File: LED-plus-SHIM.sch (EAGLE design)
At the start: 304 parts, among them IC1 TXB0101DCKR

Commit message: Fixed some texts
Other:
- note added: "PI-LEDPS-0010"
- note added: "Pi Plus sized LED-SHIM for Pi's 40-pin extension slot (c) Andriy Golovnya"
- note removed: "PI-LEDZS-0010"
- note removed: "Pi Zero sized LED-SHIM for Pi's 40-pin extension slot (c) Andriy Golovnya"
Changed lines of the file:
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@@
 <plain>
 <text x="256.54" y="7.62" size="2.54" layer="94">1.0</text>
-<text x="198.12" y="7.62" size="2.54" layer="94">PI-LEDZS-0010</text>
-<text x="165.1" y="25.4" size="2.54" layer="94">Pi Zero sized LED-SHIM for Pi's 40-pin extension slot
+<text x="198.12" y="7.62" size="2.54" layer="94">PI-LEDPS-0010</text>
+<text x="165.1" y="25.4" size="2.54" layer="94">Pi Plus sized LED-SHIM for Pi's 40-pin extension slot
 (c) Andriy Golovnya</text>
 <text x="25.4" y="121.92" size="2.54" layer="94">Right connector
@@
 <plain>
 <text x="256.54" y="7.62" size="2.54" layer="94">1.0</text>
-<text x="198.12" y="7.62" size="2.54" layer="94">PI-LEDZS-0010</text>
-<text x="165.1" y="25.4" size="2.54" layer="94">Pi Zero sized LED-SHIM for Pi's 40-pin extension slot
+<text x="198.12" y="7.62" size="2.54" layer="94">PI-LEDPS-0010</text>
+<text x="165.1" y="25.4" size="2.54" layer="94">Pi Plus sized LED-SHIM for Pi's 40-pin extension slot
 (c) Andriy Golovnya</text>
 <text x="10.16" y="86.36" size="1.778" layer="97">Following configurations are supported:
@@
 <plain>
 <text x="256.54" y="7.62" size="2.54" layer="94">1.0</text>
-<text x="198.12" y="7.62" size="2.54" layer="94">PI-LEDZS-0010</text>
-<text x="165.1" y="25.4" size="2.54" layer="94">Pi Zero sized LED-SHIM for Pi's 40-pin extension slot
+<text x="198.12" y="7.62" size="2.54" layer="94">PI-LEDPS-0010</text>
+<text x="165.1" y="25.4" size="2.54" layer="94">Pi Plus sized LED-SHIM for Pi's 40-pin extension slot
 (c) Andriy Golovnya</text>
 </plain>
@@
 <plain>
 <text x="256.54" y="7.62" size="2.54" layer="94">1.0</text>
-<text x="198.12" y="7.62" size="2.54" layer="94">PI-LEDZS-0010</text>
-<text x="165.1" y="25.4" size="2.54" layer="94">Pi Zero sized LED-SHIM for Pi's 40-pin extension slot
+<text x="198.12" y="7.62" size="2.54" layer="94">PI-LEDPS-0010</text>
+<text x="165.1" y="25.4" size="2.54" layer="94">Pi Plus sized LED-SHIM for Pi's 40-pin extension slot
 (c) Andriy Golovnya</text>
 </plain>

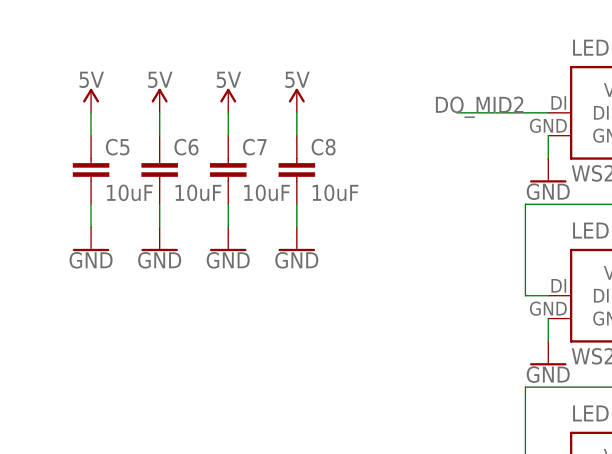
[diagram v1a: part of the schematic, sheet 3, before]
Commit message: Finished tracing plus SHIM board.
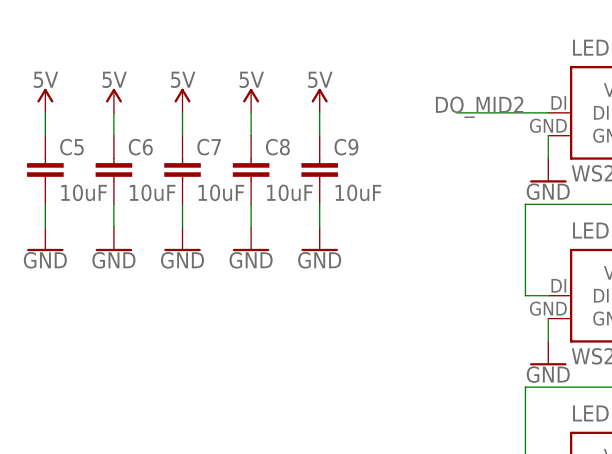
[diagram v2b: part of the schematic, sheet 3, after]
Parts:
- added C9: 10uF, rcl:C-EUC0805
- LOGO1: value MFDECLOGO_L_30MM -> MFDECLOGO_L_40MM; device _my_logos:MFDECLOGO_L_30MM -> _my_logos:MFDECLOGO_L_40MM
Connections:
- net 5V: now also C9.1
- net GND: now also C9.2
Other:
- moved on the sheet: C5, C6, C7, C8
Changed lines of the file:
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@@
 <parts>
 <part name="FRAME1" library="frames" library_urn="urn:adsk.eagle:library:229" deviceset="DINA4_L" device=""/>
-<part name="LOGO1" library="_my_logos" deviceset="MFDECLOGO" device="_L_30MM"/>
+<part name="LOGO1" library="_my_logos" deviceset="MFDECLOGO" device="_L_40MM" value="MFDECLOGO_L_40MM"/>
 <part name="SUPPLY1" library="SparkFun-PowerSymbols" library_urn="urn:adsk.eagle:library:530" deviceset="5V" device=""/>
 <part name="GND1" library="SparkFun-PowerSymbols" library_urn="urn:adsk.eagle:library:530" deviceset="GND" device=""/>
@@
 <part name="SUPPLY304" library="SparkFun-PowerSymbols" library_urn="urn:adsk.eagle:library:530" deviceset="5V" device=""/>
 <part name="GND301" library="SparkFun-PowerSymbols" library_urn="urn:adsk.eagle:library:530" deviceset="GND" device=""/>
+<part name="C9" library="rcl" library_urn="urn:adsk.eagle:library:334" deviceset="C-EU" device="C0805" package3d_urn="urn:adsk.eagle:package:23617/2" value="10uF"/>
+<part name="SUPPLY305" library="SparkFun-PowerSymbols" library_urn="urn:adsk.eagle:library:530" deviceset="5V" device=""/>
+<part name="GND302" library="SparkFun-PowerSymbols" library_urn="urn:adsk.eagle:library:530" deviceset="GND" device=""/>
 </parts>
 <sheets>
@@
 <attribute name="VALUE" x="124.46" y="9.906" size="1.778" layer="96" align="top-center"/>
 </instance>
-<instance part="C5" gate="G$1" x="20.32" y="154.94" smashed="yes">
-<attribute name="NAME" x="21.844" y="155.321" size="1.778" layer="95"/>
-<attribute name="VALUE" x="21.844" y="150.241" size="1.778" layer="96"/>
+<instance part="C5" gate="G$1" x="15.24" y="154.94" smashed="yes">
+<attribute name="NAME" x="16.764" y="155.321" size="1.778" layer="95"/>
+<attribute name="VALUE" x="16.764" y="150.241" size="1.778" layer="96"/>
 </instance>
-<instance part="SUPPLY301" gate="G$1" x="20.32" y="160.02" smashed="yes">
-<attribute name="VALUE" x="20.32" y="162.814" size="1.778" layer="96" align="bottom-center"/>
+<instance part="SUPPLY301" gate="G$1" x="15.24" y="160.02" smashed="yes">
+<attribute name="VALUE" x="15.24" y="162.814" size="1.778" layer="96" align="bottom-center"/>
 </instance>
-<instance part="GND298" gate="1" x="20.32" y="144.78" smashed="yes">
-<attribute name="VALUE" x="20.32" y="144.526" size="1.778" layer="96" align="top-center"/>
+<instance part="GND298" gate="1" x="15.24" y="144.78" smashed="yes">
+<attribute name="VALUE" x="15.24" y="144.526" size="1.778" layer="96" align="top-center"/>
 </instance>
-<instance part="C6" gate="G$1" x="27.94" y="154.94" smashed="yes">
-<attribute name="NAME" x="29.464" y="155.321" size="1.778" layer="95"/>
-<attribute name="VALUE" x="29.464" y="150.241" size="1.778" layer="96"/>
+<instance part="C6" gate="G$1" x="22.86" y="154.94" smashed="yes">
+<attribute name="NAME" x="24.384" y="155.321" size="1.778" layer="95"/>
+<attribute name="VALUE" x="24.384" y="150.241" size="1.778" layer="96"/>
 </instance>
-<instance part="SUPPLY302" gate="G$1" x="27.94" y="160.02" smashed="yes">
-<attribute name="VALUE" x="27.94" y="162.814" size="1.778" layer="96" align="bottom-center"/>
+<instance part="SUPPLY302" gate="G$1" x="22.86" y="160.02" smashed="yes">
+<attribute name="VALUE" x="22.86" y="162.814" size="1.778" layer="96" align="bottom-center"/>
 </instance>
-<instance part="GND299" gate="1" x="27.94" y="144.78" smashed="yes">
-<attribute name="VALUE" x="27.94" y="144.526" size="1.778" layer="96" align="top-center"/>
+<instance part="GND299" gate="1" x="22.86" y="144.78" smashed="yes">
+<attribute name="VALUE" x="22.86" y="144.526" size="1.778" layer="96" align="top-center"/>
 </instance>
-<instance part="C7" gate="G$1" x="35.56" y="154.94" smashed="yes">
-<attribute name="NAME" x="37.084" y="155.321" size="1.778" layer="95"/>
-<attribute name="VALUE" x="37.084" y="150.241" size="1.778" layer="96"/>
+<instance part="C7" gate="G$1" x="30.48" y="154.94" smashed="yes">
+<attribute name="NAME" x="32.004" y="155.321" size="1.778" layer="95"/>
+<attribute name="VALUE" x="32.004" y="150.241" size="1.778" layer="96"/>
 </instance>
-<instance part="SUPPLY303" gate="G$1" x="35.56" y="160.02" smashed="yes">
-<attribute name="VALUE" x="35.56" y="162.814" size="1.778" layer="96" align="bottom-center"/>
+<instance part="SUPPLY303" gate="G$1" x="30.48" y="160.02" smashed="yes">
+<attribute name="VALUE" x="30.48" y="162.814" size="1.778" layer="96" align="bottom-center"/>
 </instance>
-<instance part="GND300" gate="1" x="35.56" y="144.78" smashed="yes">
-<attribute name="VALUE" x="35.56" y="144.526" size="1.778" layer="96" align="top-center"/>
+<instance part="GND300" gate="1" x="30.48" y="144.78" smashed="yes">
+<attribute name="VALUE" x="30.48" y="144.526" size="1.778" layer="96" align="top-center"/>
 </instance>
-<instance part="C8" gate="G$1" x="43.18" y="154.94" smashed="yes">
-<attribute name="NAME" x="44.704" y="155.321" size="1.778" layer="95"/>
-<attribute name="VALUE" x="44.704" y="150.241" size="1.778" layer="96"/>
+<instance part="C8" gate="G$1" x="38.1" y="154.94" smashed="yes">
+<attribute name="NAME" x="39.624" y="155.321" size="1.778" layer="95"/>
+<attribute name="VALUE" x="39.624" y="150.241" size="1.778" layer="96"/>
 </instance>
-<instance part="SUPPLY304" gate="G$1" x="43.18" y="160.02" smashed="yes">
-<attribute name="VALUE" x="43.18" y="162.814" size="1.778" layer="96" align="bottom-center"/>
+<instance part="SUPPLY304" gate="G$1" x="38.1" y="160.02" smashed="yes">
+<attribute name="VALUE" x="38.1" y="162.814" size="1.778" layer="96" align="bottom-center"/>
 </instance>
-<instance part="GND301" gate="1" x="43.18" y="144.78" smashed="yes">
-<attribute name="VALUE" x="43.18" y="144.526" size="1.778" layer="96" align="top-center"/>
+<instance part="GND301" gate="1" x="38.1" y="144.78" smashed="yes">
+<attribute name="VALUE" x="38.1" y="144.526" size="1.778" layer="96" align="top-center"/>
+</instance>
+<instance part="C9" gate="G$1" x="45.72" y="154.94" smashed="yes">
+<attribute name="NAME" x="47.244" y="155.321" size="1.778" layer="95"/>
+<attribute name="VALUE" x="47.244" y="150.241" size="1.778" layer="96"/>
+</instance>
+<instance part="SUPPLY305" gate="G$1" x="45.72" y="160.02" smashed="yes">
+<attribute name="VALUE" x="45.72" y="162.814" size="1.778" layer="96" align="bottom-center"/>
+</instance>
+<instance part="GND302" gate="1" x="45.72" y="144.78" smashed="yes">
+<attribute name="VALUE" x="45.72" y="144.526" size="1.778" layer="96" align="top-center"/>
 </instance>
 </instances>
@@
 <segment>
 <pinref part="C5" gate="G$1" pin="1"/>
-<wire x1="20.32" y1="157.48" x2="20.32" y2="160.02" width="0.1524" layer="91"/>
+<wire x1="15.24" y1="157.48" x2="15.24" y2="160.02" width="0.1524" layer="91"/>
 <pinref part="SUPPLY301" gate="G$1" pin="5V"/>
 </segment>
 <segment>
 <pinref part="C6" gate="G$1" pin="1"/>
-<wire x1="27.94" y1="157.48" x2="27.94" y2="160.02" width="0.1524" layer="91"/>
+<wire x1="22.86" y1="157.48" x2="22.86" y2="160.02" width="0.1524" layer="91"/>
 <pinref part="SUPPLY302" gate="G$1" pin="5V"/>
 </segment>
 <segment>
 <pinref part="C7" gate="G$1" pin="1"/>
-<wire x1="35.56" y1="157.48" x2="35.56" y2="160.02" width="0.1524" layer="91"/>
+<wire x1="30.48" y1="157.48" x2="30.48" y2="160.02" width="0.1524" layer="91"/>
 <pinref part="SUPPLY303" gate="G$1" pin="5V"/>
 </segment>
 <segment>
 <pinref part="C8" gate="G$1" pin="1"/>
-<wire x1="43.18" y1="157.48" x2="43.18" y2="160.02" width="0.1524" layer="91"/>
+<wire x1="38.1" y1="157.48" x2="38.1" y2="160.02" width="0.1524" layer="91"/>
 <pinref part="SUPPLY304" gate="G$1" pin="5V"/>
 </segment>
+<segment>
+<pinref part="C9" gate="G$1" pin="1"/>
+<wire x1="45.72" y1="157.48" x2="45.72" y2="160.02" width="0.1524" layer="91"/>
+<pinref part="SUPPLY305" gate="G$1" pin="5V"/>
+</segment>
 </net>
 <net name="GND" class="0">
@@
 <segment>
 <pinref part="C5" gate="G$1" pin="2"/>
-<wire x1="20.32" y1="149.86" x2="20.32" y2="147.32" width="0.1524" layer="91"/>
+<wire x1="15.24" y1="149.86" x2="15.24" y2="147.32" width="0.1524" layer="91"/>
 <pinref part="GND298" gate="1" pin="GND"/>
 </segment>
 <segment>
 <pinref part="C6" gate="G$1" pin="2"/>
-<wire x1="27.94" y1="149.86" x2="27.94" y2="147.32" width="0.1524" layer="91"/>
+<wire x1="22.86" y1="149.86" x2="22.86" y2="147.32" width="0.1524" layer="91"/>
 <pinref part="GND299" gate="1" pin="GND"/>
 </segment>
 <segment>
 <pinref part="C7" gate="G$1" pin="2"/>
-<wire x1="35.56" y1="149.86" x2="35.56" y2="147.32" width="0.1524" layer="91"/>
+<wire x1="30.48" y1="149.86" x2="30.48" y2="147.32" width="0.1524" layer="91"/>
 <pinref part="GND300" gate="1" pin="GND"/>
 </segment>
 <segment>
 <pinref part="C8" gate="G$1" pin="2"/>
-<wire x1="43.18" y1="149.86" x2="43.18" y2="147.32" width="0.1524" layer="91"/>
+<wire x1="38.1" y1="149.86" x2="38.1" y2="147.32" width="0.1524" layer="91"/>
 <pinref part="GND301" gate="1" pin="GND"/>
 </segment>
+<segment>
+<pinref part="C9" gate="G$1" pin="2"/>
+<wire x1="45.72" y1="149.86" x2="45.72" y2="147.32" width="0.1524" layer="91"/>
+<pinref part="GND302" gate="1" pin="GND"/>
+</segment>
 </net>
